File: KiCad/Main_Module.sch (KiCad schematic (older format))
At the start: 44 parts, among them Q1 Q_NMOS_GDS, Q2 Q_NMOS_GDS, Q3 Q_NMOS_GDS, Q4 Q_NMOS_GDS, U1 LM324

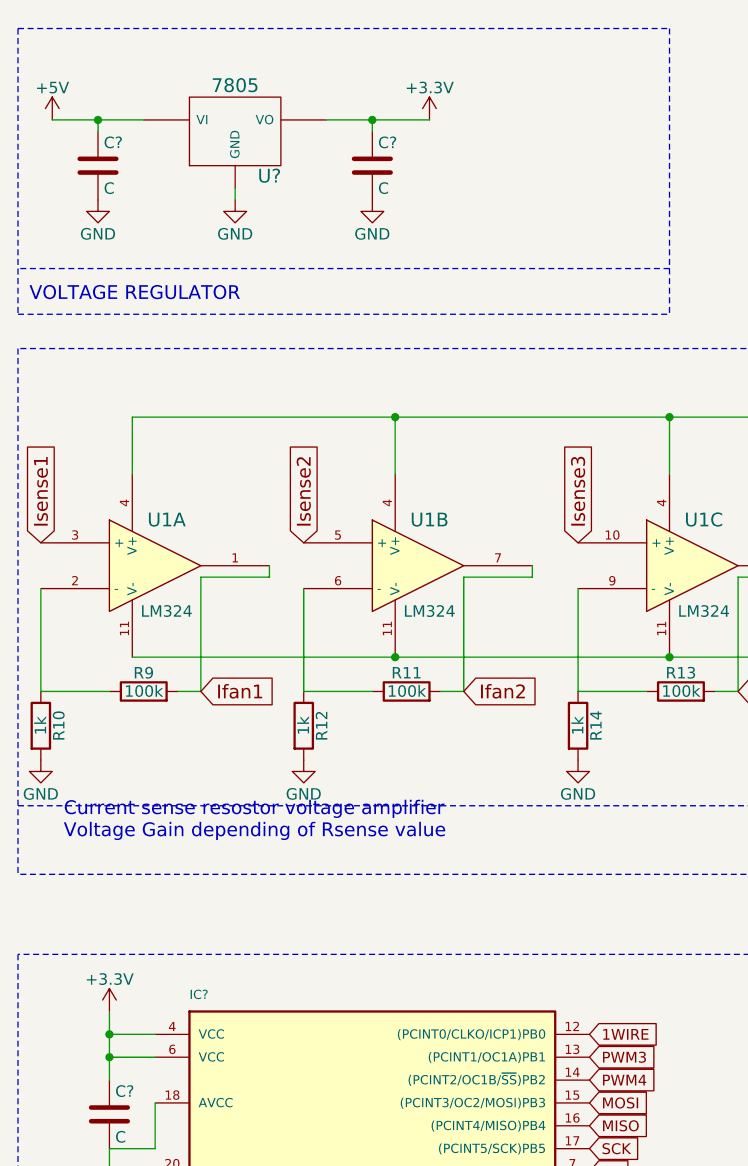
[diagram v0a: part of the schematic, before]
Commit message: User Module added
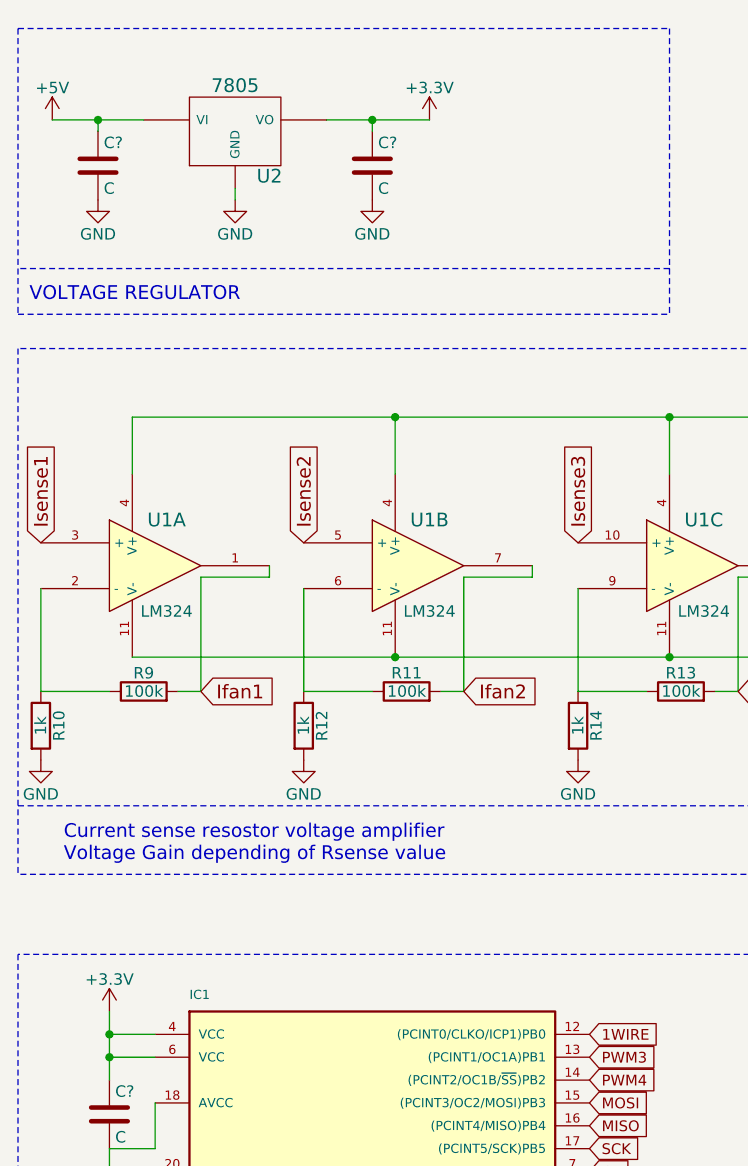
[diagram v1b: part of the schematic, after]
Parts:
- gave numbers to parts that had none: 2
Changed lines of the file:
@@
 LIBS:contrib
 LIBS:valves
-LIBS:FANCRT-cache
-EELAYER 27 0
+LIBS:Main_Module-cache
+EELAYER 25 0
 EELAYER END
 $Descr A4 11693 8268
@@
 $EndDescr
 $Comp
-L ATMEGA88-A IC?
+L ATMEGA88-A IC1
 U 1 1 55B482E8
 P 2050 6050
-F 0 "IC?" H 1300 7300 40  0000 L BNN
+F 0 "IC1" H 1300 7300 40  0000 L BNN
 F 1 "ATMEGA88-A" H 2500 4650 40  0000 L BNN
 F 2 "TQFP32" H 2050 6050 30  0000 C CIN
@@
 Wire Notes Line
 	550  1950 550  4250
-Text Notes 750  4100 0    60   ~ 0
+Text Notes 750  4200 0    60   ~ 0
 Current sense resostor voltage amplifier\nVoltage Gain depending of Rsense value
 $Comp
@@
 	5500 4250 550  4250
 $Comp
-L 7805 U?
+L 7805 U2
 U 1 1 55B4C891
 P 1500 1000
-F 0 "U?" H 1650 804 60  0000 C CNN
+F 0 "U2" H 1650 804 60  0000 C CNN
 F 1 "7805" H 1500 1200 60  0000 C CNN
 F 2 "" H 1500 1000 60  0000 C CNN

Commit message: some changes on mainmodule
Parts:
- added FAN1Header2: CONN_01X03, symbol CONN_01X03
- renumbered FAN1Header to FAN1Header1, FAN2Header to FAN2Header1, FAN3Header to FAN3Header1, FAN4Header to FAN4Header1
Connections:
- net +12V: now also FAN1Header2.2 (P2)
- net FAN1: now also FAN1Header2.1 (P1)
- net TACHO1: no longer FAN1Header1.3 (P3)
- new net TACHO1_1: FAN1Header1.3 (P3)
- new net TACHO1_2: FAN1Header2.3 (P3)
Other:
- moved on the sheet: D1, D2, D3, D4, FAN1Header1, FAN2Header1, FAN3Header1, FAN4Header1, ISP Header, R10, R11, R12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
